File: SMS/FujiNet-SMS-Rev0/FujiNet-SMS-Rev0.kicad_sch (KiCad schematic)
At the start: 0 parts

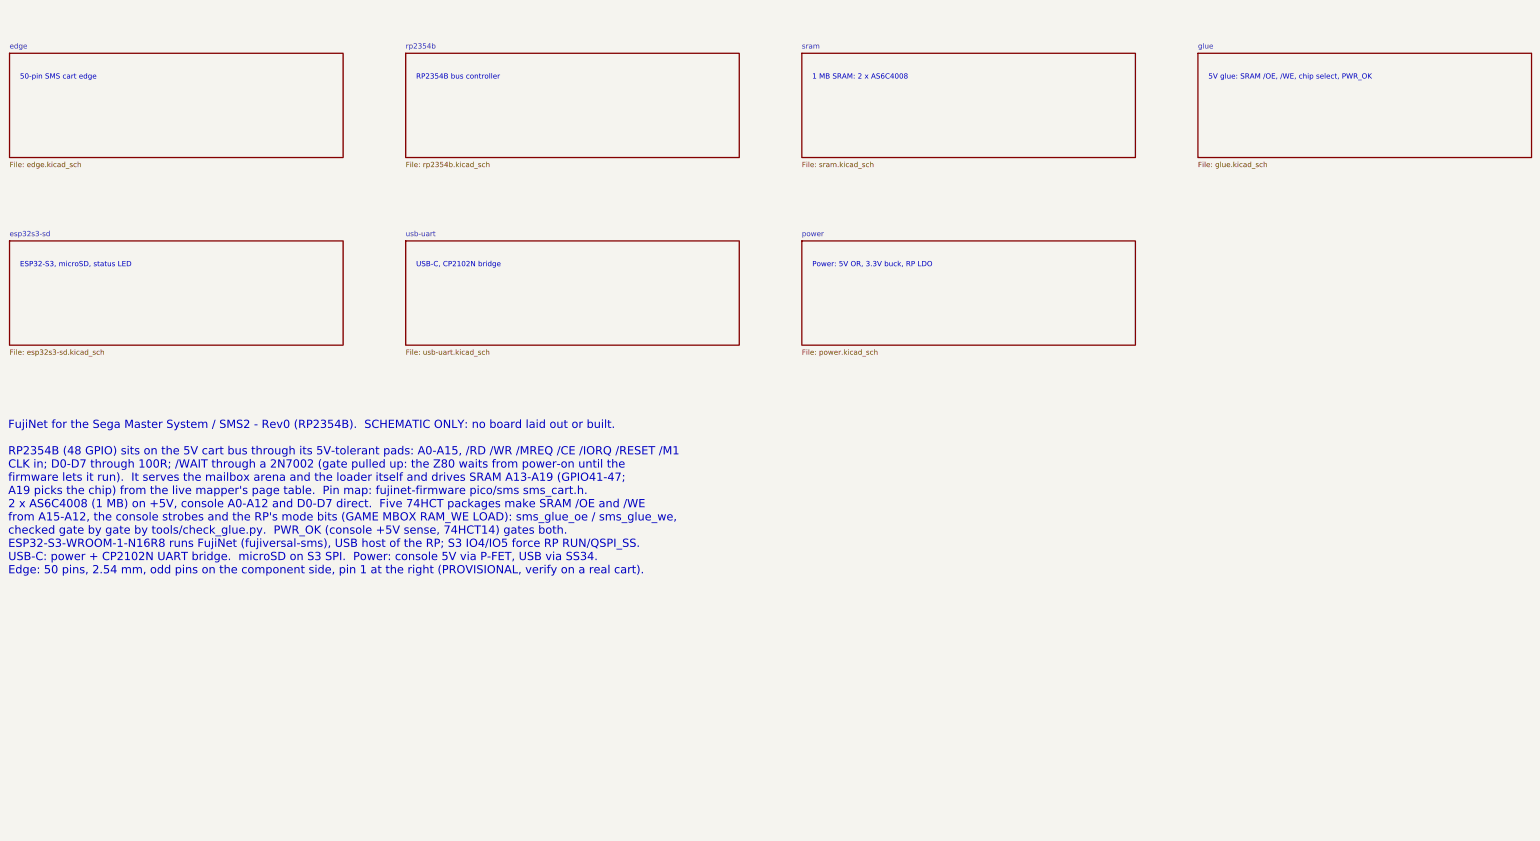
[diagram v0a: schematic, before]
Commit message: SMS Rev0: co-designed 6-layer board, board-mirroring schematic, JLCPCB + PCBWay packages (#52)
* SMS Rev0: audit with kicad-happy + datasheets, fix the edge, redraw the schematic

Edge connector: every source (SMS Power slot diagram, little-scale, a 171-5519
scan, raphnet, the barbeque and reidrac footprints) puts the EVEN pins on the
component / label side with pins 1/2 at the right.  The schematic-only
footprint had the faces swapped, which would have put console +5V on /WR.
make_edge_fp.py now writes even pads on F.Cu, odd on B.Cu, 1.75 x 8.75 mm
fingers 0.75-9.5 mm from the edge on a 65.8 mm tab; check_nets.py asserts it
and tools/audit/edge_orientation.py checks it against the sources.

kicad-happy + datasheet audit (docs/design-review-rev0.md Part 1, 27 deep
review findings, gate 27/27): R_VBPD 4.7k VBUS pull-down (SS34 leakage lifts
the P-FET gate), /WAIT gate pull-up 10k -> 4.7k (GPIO34's reset pull-down vs
the 2N7002's 2.5 V threshold), 10 uF bulk on the console 5V.

Schematic: hierarchical sheets wired on a root block diagram (edge -> RP2354B
-> ESP32-S3 -> USB, glue and SRAM under the RP, power below); every sheet
drawn left to right, the glue as a wired logic network by gate depth, the
RP2354B mirrored so its bus faces the console, small sheets on A4.  Parts
are addressed by key (design.py), no more NES reference aliasing.  sch_draw
gains hierarchical labels, sheet blocks, a bus graph and flag / power-pin
lints; gen_sch checks the hierarchy against design.py and names nets by
their last path element (one bus vector per bus: KiCad joins differing
vectors by position).  ERC 0, check_nets 437/437, check_glue 8192/8192.

JLC CPL rotations measured against the EasyEDA footprint of every LCSC part
(tools/audit/jlc); the AS6C4008 has no EasyEDA footprint.

Co-Authored-By: Claude Opus 5.5 <noreply@anthropic.com>

* SMS Rev0: board pipeline, placement and cartridge shell (WIP, not routed yet)

The NES Rev0 6-layer pipeline ported to SMS (gen_pcb, fanout, Freerout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
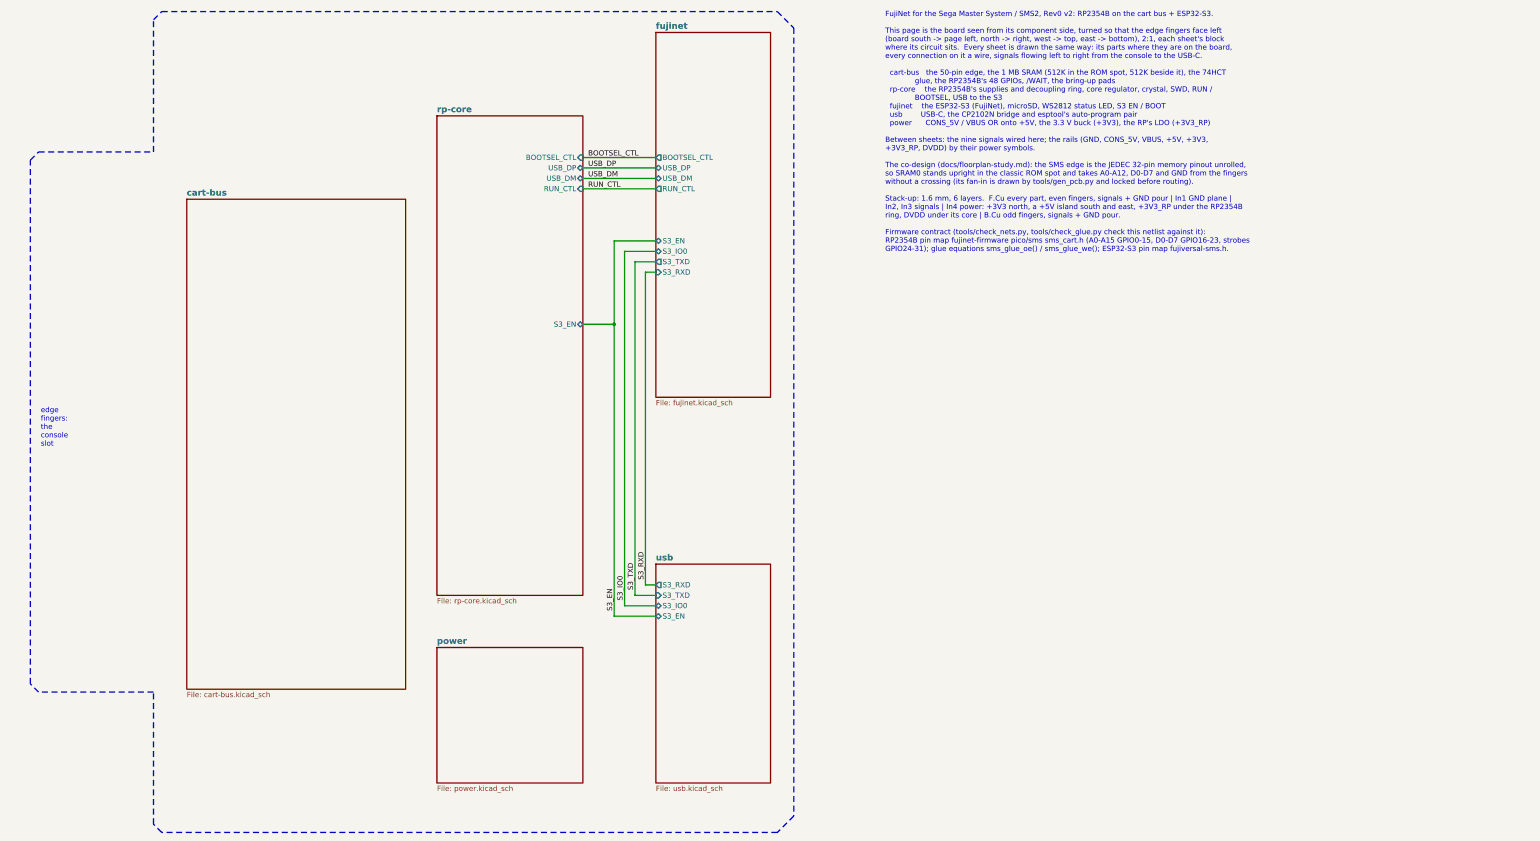
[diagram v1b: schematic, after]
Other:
- removed sheet edge
- removed sheet esp32s3-sd
- removed sheet glue
- removed sheet rp2354b
- removed sheet sram
- removed sheet usb-uart
- added sheet cart-bus (cart-bus.kicad_sch)
- added sheet fujinet (fujinet.kicad_sch)
- added sheet rp-core (rp-core.kicad_sch)
- added sheet usb (usb.kicad_sch)
- note added: "FujiNet for the Sega Master System / SMS2, Rev0 v2: RP2354B on the cart bus + ESP32-S3. This page is the board seen from its component side, turned so that the edge fingers face left (board south -> page left, north -> right, west -> top, east -> bottom), 2:1, each sheet's block where its circuit sits. Every sheet is drawn the same way: its parts where they are on the board, every connection on i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"
- note added: "edge fingers: the console slot"
- note removed: "1 MB SRAM: 2 x AS6C4008"
- note removed: "50-pin SMS cart edge"
- note removed: "5V glue: SRAM /OE, /WE, chip select, PWR_OK"
- note removed: "ESP32-S3, microSD, status LED"
- note removed: "FujiNet for the Sega Master System / SMS2 - Rev0 (RP2354B). SCHEMATIC ONLY: no board laid out or built. RP2354B (48 GPIO) sits on the 5V cart bus through its 5V-tolerant pads: A0-A15, /RD /WR /MREQ /CE /IORQ /RESET /M1 CLK in; D0-D7 through 100R; /WAIT through a 2N7002 (gate pulled up: the Z80 waits from power-on until the firmware lets it run). It serves the mailbox arena and the loader itself a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"
- note removed: "Power: 5V OR, 3.3V buck, RP LDO"
- note removed: "RP2354B bus controller"
- note removed: "USB-C, CP2102N bridge"
